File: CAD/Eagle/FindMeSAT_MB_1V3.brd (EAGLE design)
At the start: 99 x 49.2 mm, 135 parts, among them Q101 ABS07-32.768KHZ, Q651 ABM3B-16MHZ-10-R50-1-U, U1001 CFPT-141-20MHZ, U101 ATXMEGA256A3BU-AU, U1011 OPA354, U1021 OPA354, U1111 LM2831YMF, U1121 LM4120IM5-3.0, U201 SIM808, U301 MPU-9250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

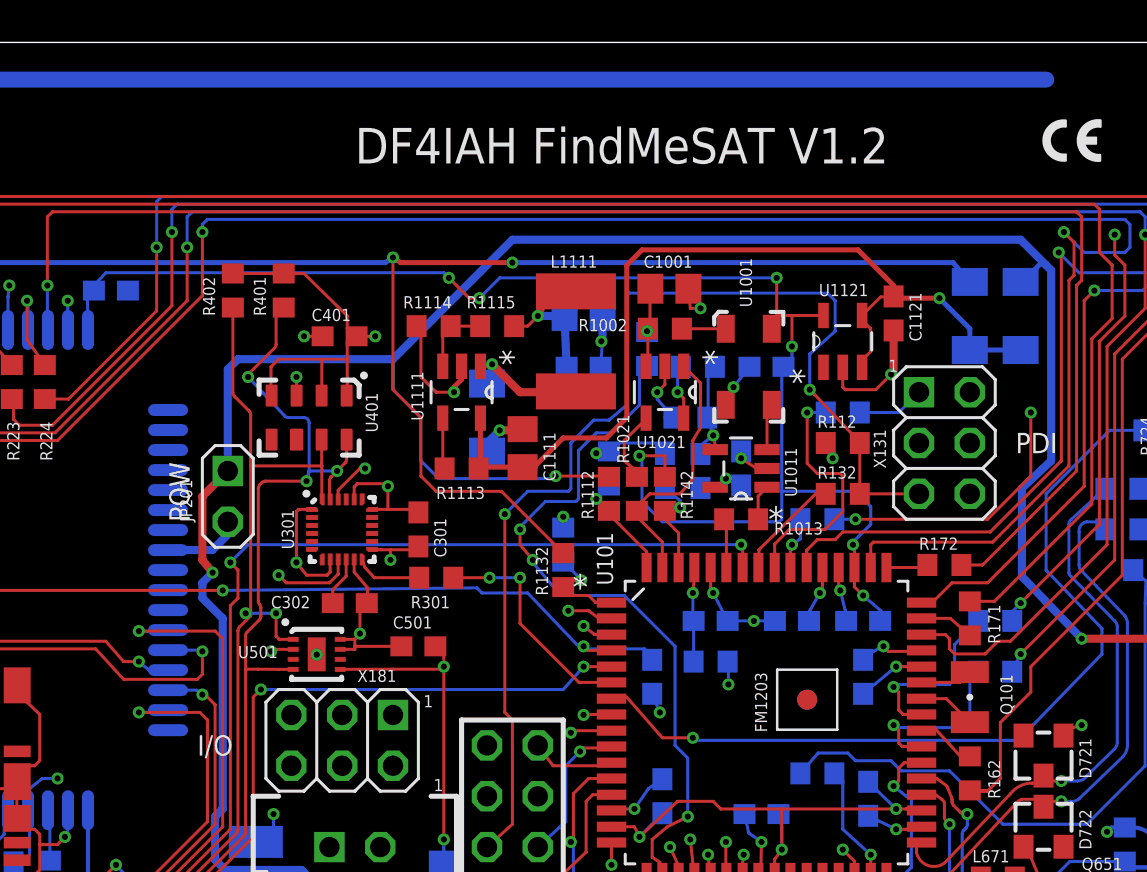
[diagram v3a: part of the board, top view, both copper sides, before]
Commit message: HW_V1.3 - Version strings changed to V1.3, missing C302 with 10nF added, missing GND vias for U201 added (4x)
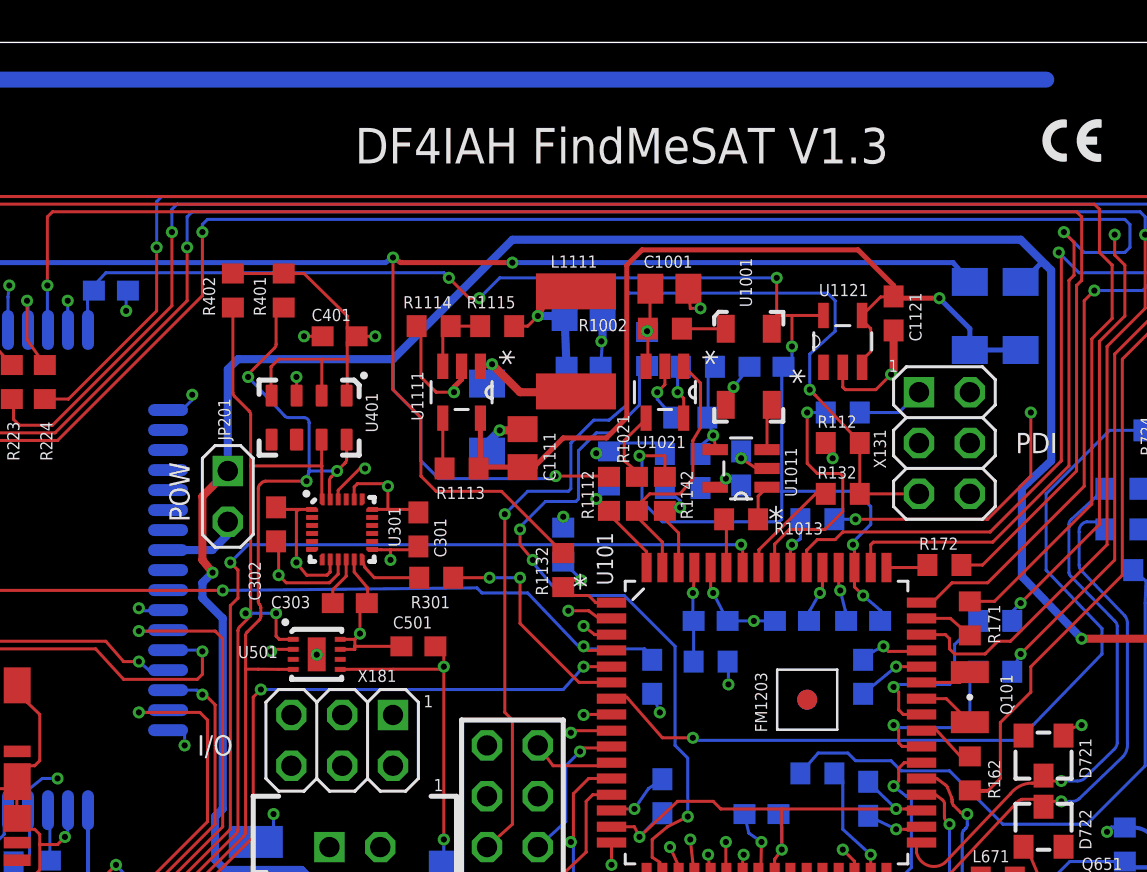
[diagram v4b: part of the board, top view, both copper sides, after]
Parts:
- added C303: 100nF, rcl:C0603
- C302: value 100nF -> 10nF
- moved C302 5.39 mm to (46.6, 25.1), turned to 270 degrees
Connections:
- net +3V3: now also C302.1
- net GAM_RO: now also C303.1; no longer C302.1
- net GND: now also C303.2
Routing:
- net GND: track 230.1 -> 234.7 mm, vias 69 -> 73
- net +3V3: track 103.5 -> 104.4 mm
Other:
- board text added: "DF4IAH FindMeSAT V1.3"
- board text removed: "DF4IAH FindMeSAT V1.2"
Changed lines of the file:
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@@
 <layer number="19" name="Unrouted" color="6" fill="1" visible="yes" active="yes"/>
 <layer number="20" name="Dimension" color="15" fill="1" visible="yes" active="yes"/>
-<layer number="21" name="tPlace" color="7" fill="1" visible="no" active="yes"/>
+<layer number="21" name="tPlace" color="7" fill="1" visible="yes" active="yes"/>
 <layer number="22" name="bPlace" color="7" fill="1" visible="yes" active="yes"/>
-<layer number="23" name="tOrigins" color="15" fill="1" visible="no" active="yes"/>
+<layer number="23" name="tOrigins" color="15" fill="1" visible="yes" active="yes"/>
 <layer number="24" name="bOrigins" color="15" fill="1" visible="yes" active="yes"/>
-<layer number="25" name="tNames" color="7" fill="1" visible="no" active="yes"/>
-<layer number="26" name="bNames" color="7" fill="1" visible="no" active="yes"/>
+<layer number="25" name="tNames" color="7" fill="1" visible="yes" active="yes"/>
+<layer number="26" name="bNames" color="7" fill="1" visible="yes" active="yes"/>
 <layer number="27" name="tValues" color="5" fill="1" visible="no" active="yes"/>
 <layer number="28" name="bValues" color="5" fill="1" visible="no" active="yes"/>
-<layer number="29" name="tStop" color="7" fill="3" visible="no" active="yes"/>
+<layer number="29" name="tStop" color="7" fill="3" visible="yes" active="yes"/>
 <layer number="30" name="bStop" color="7" fill="6" visible="yes" active="yes"/>
 <layer number="31" name="tCream" color="7" fill="4" visible="no" active="yes"/>
-<layer number="32" name="bCream" color="7" fill="5" visible="yes" active="yes"/>
+<layer number="32" name="bCream" color="7" fill="5" visible="no" active="yes"/>
 <layer number="33" name="tFinish" color="6" fill="3" visible="no" active="yes"/>
 <layer number="34" name="bFinish" color="6" fill="6" visible="no" active="yes"/>
@@
 <layer number="50" name="dxf" color="7" fill="1" visible="no" active="no"/>
 <layer number="51" name="tDocu" color="7" fill="1" visible="no" active="yes"/>
-<layer number="52" name="bDocu" color="7" fill="1" visible="yes" active="yes"/>
+<layer number="52" name="bDocu" color="7" fill="1" visible="no" active="yes"/>
 <layer number="53" name="tGND_GNDA" color="7" fill="9" visible="no" active="no"/>
 <layer number="54" name="bGND_GNDA" color="1" fill="9" visible="no" active="no"/>
@@
 <dimension x1="99.04" y1="49.23" x2="99.04" y2="0" x3="-2.54" y3="24.615" textsize="1.778" layer="47"/>
 <dimension x1="99.06" y1="0" x2="0" y2="0" x3="49.53" y3="52.07" textsize="1.778" layer="47"/>
-<text x="50.546" y="43.18" size="1.778" layer="21">DF4IAH FindMeSAT V1.2</text>
+<text x="50.546" y="43.18" size="1.778" layer="21">DF4IAH FindMeSAT V1.3</text>
 <text x="77.216" y="32.766" size="0.6096" layer="21" ratio="20">1</text>
 <text x="61.468" y="3.048" size="0.6096" layer="21" ratio="20">1</text>
@@
 <text x="88.9" y="43.18" size="1.016" layer="2" ratio="12">DF4IAH
 FindMeSAT
-V1.2</text>
+V1.3</text>
 <text x="95.504" y="43.18" size="0.8128" layer="2" ratio="10" rot="R90">L2</text>
 <text x="96.647" y="43.18" size="0.8128" layer="16" rot="MR90">L4</text>
@@
 </element>
 <element name="U301" library="df4iah_sensors" package="QFN24-3X3" value="MPU-9250" x="49.911" y="24.892" smashed="yes">
-<attribute name="NAME" x="47.498" y="24.892" size="0.6096" layer="25" font="vector" ratio="10" rot="R90" align="bottom-center"/>
+<attribute name="NAME" x="52.832" y="25.019" size="0.6096" layer="25" font="vector" ratio="10" rot="R90" align="bottom-center"/>
 <attribute name="VALUE" x="49.276" y="25.146" size="0.6096" layer="27" font="vector" rot="R90" align="top-center"/>
 </element>
@@
 <attribute name="VALUE" x="54.102" y="23.749" size="0.6096" layer="27" rot="R90"/>
 </element>
-<element name="C302" library="rcl" package="C0603" value="100nF" x="50.292" y="21.209" smashed="yes">
+<element name="C303" library="rcl" package="C0603" value="100nF" x="50.292" y="21.209" smashed="yes">
 <attribute name="NAME" x="46.355" y="20.955" size="0.6096" layer="25"/>
 <attribute name="VALUE" x="49.53" y="20.828" size="0.6096" layer="27"/>
@@
 </element>
 <element name="JP201" library="df4iah_connector" package="1X02" value="POW" x="44.196" y="27.813" smashed="yes" rot="R180">
-<attribute name="NAME" x="42.418" y="25.273" size="0.6096" layer="25" ratio="10" rot="R90"/>
+<attribute name="NAME" x="44.323" y="29.337" size="0.6096" layer="25" ratio="10" rot="R90"/>
 <attribute name="VALUE" x="46.736" y="30.988" size="1.27" layer="27" rot="R180"/>
 </element>
@@
 <attribute name="VALUE" x="64.135" y="27.178" size="0.6096" layer="28" rot="MR90"/>
 </element>
+<element name="C302" library="rcl" package="C0603" value="10nF" x="46.609" y="25.146" smashed="yes" rot="R270">
+<attribute name="NAME" x="45.847" y="21.336" size="0.6096" layer="25" rot="R90"/>
+<attribute name="VALUE" x="46.355" y="26.162" size="0.6096" layer="27" rot="R270"/>
+</element>
 </elements>
 <signals>
@@
 <contactref element="U301" pad="18"/>
 <contactref element="U301" pad="11"/>
-<contactref element="C302" pad="2"/>
+<contactref element="C303" pad="2"/>
 <contactref element="C401" pad="2"/>
 <via x="48.006" y="34.544" extent="1-16" drill="0.3048" shape="octagon"/>
@@
 <via x="86.995" y="1.524" extent="1-16" drill="0.3048" shape="octagon"/>
 <via x="90.043" y="6.604" extent="1-16" drill="0.3048" shape="octagon"/>
-<wire x1="50.546" y1="18.89921875" x2="50.546" y2="18.415" width="0" layer="19" extent="1-16"/>
 <wire x1="45.212" y1="3.81" x2="42.545" y2="3.81" width="0.1524" layer="16"/>
 <wire x1="41.91" y1="3.048" x2="42.545" y2="3.81" width="0.1524" layer="16"/>
@@
 <via x="6.50744375" y="8.4978875" extent="1-16" drill="0.3048" shape="octagon"/>
 <contactref element="C1141" pad="2"/>
+<contactref element="C302" pad="2"/>
+<wire x1="46.736" y1="24.003" x2="46.736" y2="22.606" width="0.1524" layer="1"/>
 <wire x1="93.384" y1="32.258" x2="94.996" y2="38.1" width="0" layer="19" extent="16-16"/>
 <wire x1="93.025" y1="22.225" x2="94.23" y2="29.24" width="0" layer="19" extent="1-1"/>
@@
 <wire x1="50.511" y1="23.392" x2="51.4635" y2="25.892" width="0" layer="19" extent="1-1"/>
 <wire x1="49.711" y1="23.392" x2="50.511" y2="23.392" width="0" layer="19" extent="1-1"/>
+<wire x1="46.609" y1="24.296" x2="46.736" y2="24.003" width="0" layer="19" extent="1-1"/>
 <wire x1="48.638590625" y1="18.64921875" x2="49.813590625" y2="18.89921875" width="0" layer="19" extent="1-1"/>
 <wire x1="48.641" y1="18.634" x2="48.638590625" y2="18.64921875" width="0" layer="19" extent="1-1"/>
 <wire x1="47.463590625" y1="18.89921875" x2="48.638590625" y2="18.64921875" width="0" layer="19" extent="1-1"/>
-<wire x1="52.451" y1="15.621" x2="50.546" y2="18.415" width="0" layer="19" extent="1-1"/>
+<wire x1="52.451" y1="15.621" x2="52.871" y2="19.05" width="0" layer="19" extent="1-1"/>
 <wire x1="74.93" y1="32.9946" x2="70.27" y2="33.02" width="0" layer="19" extent="1-16"/>
 <wire x1="48.934" y1="34.544" x2="53.633" y2="35.052" width="0" layer="19" extent="1-1"/>
@@
 <wire x1="11.43" y1="37.973" x2="11.43" y2="38.1" width="0" layer="19" extent="1-1"/>
 <wire x1="15.66" y1="36.068" x2="15.367" y2="36.068" width="0" layer="19" extent="1-1"/>
+<via x="39.116" y="35.814" extent="1-16" drill="0.3048" shape="octagon"/>
+<via x="42.418" y="31.623" extent="1-16" drill="0.3048" shape="octagon"/>
+<via x="39.751" y="20.955" extent="1-16" drill="0.3048" shape="octagon"/>
+<wire x1="39.116" y1="35.814" x2="39.116" y2="36.703" width="0.1524" layer="16"/>
+<wire x1="42.418" y1="31.623" x2="42.418" y2="31.369" width="0.1524" layer="16"/>
+<wire x1="42.418" y1="31.369" x2="42.037" y2="30.988" width="0.1524" layer="16"/>
+<wire x1="39.751" y1="20.955" x2="39.878" y2="20.828" width="0.1524" layer="16"/>
+<wire x1="39.878" y1="20.828" x2="40.513" y2="20.828" width="0.1524" layer="16"/>
+<via x="42.037" y="14.097" extent="1-16" drill="0.3048" shape="octagon"/>
+<wire x1="42.037" y1="14.097" x2="42.037" y2="14.732" width="0.1524" layer="16"/>
 </signal>
 <signal name="EN">
@@
 <wire x1="54.991" y1="18.034" x2="54.991" y2="19.05" width="0.1524" layer="1"/>
 <contactref element="X121" pad="5"/>
+<contactref element="C302" pad="1"/>
+<wire x1="46.863" y1="25.892" x2="47.752" y2="25.892" width="0.1524" layer="1"/>
 <wire x1="74.422" y1="28.868" x2="81.28" y2="31.75" width="0" layer="19" extent="1-1"/>
 <wire x1="69.85" y1="27.09" x2="74.08" y2="29.21" width="0" layer="19" extent="1-16"/>
@@
 <wire x1="54.571" y1="19.05" x2="54.991" y2="19.05" width="0" layer="19" extent="1-1"/>
 <wire x1="49.149" y1="22.606" x2="49.813590625" y2="17.89921875" width="0" layer="19" extent="1-1"/>
+<wire x1="47.752" y1="25.892" x2="47.736" y2="25.892" width="0" layer="19" extent="1-1"/>
+<wire x1="46.609" y1="25.996" x2="46.863" y2="25.892" width="0" layer="19" extent="1-1"/>
 <wire x1="49.711" y1="26.392" x2="48.3585" y2="25.892" width="0" layer="19" extent="1-1"/>
 <wire x1="51.4635" y1="23.892" x2="49.311" y2="23.392" width="0" layer="19" extent="1-1"/>
@@
 <signal name="GAM_RO">
 <contactref element="U301" pad="10"/>
-<contactref element="C302" pad="1"/>
+<contactref element="C303" pad="1"/>
 <wire x1="50.111" y1="23.392" x2="50.111" y2="22.552" width="0.1524" layer="1"/>
 <wire x1="50.111" y1="22.552" x2="49.442" y2="21.883" width="0.1524" layer="1"/>
